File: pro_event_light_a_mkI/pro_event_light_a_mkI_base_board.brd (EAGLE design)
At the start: 39.4 x 59.4 mm, 32 parts, among them IC1 LT1936, IC2 LT1936

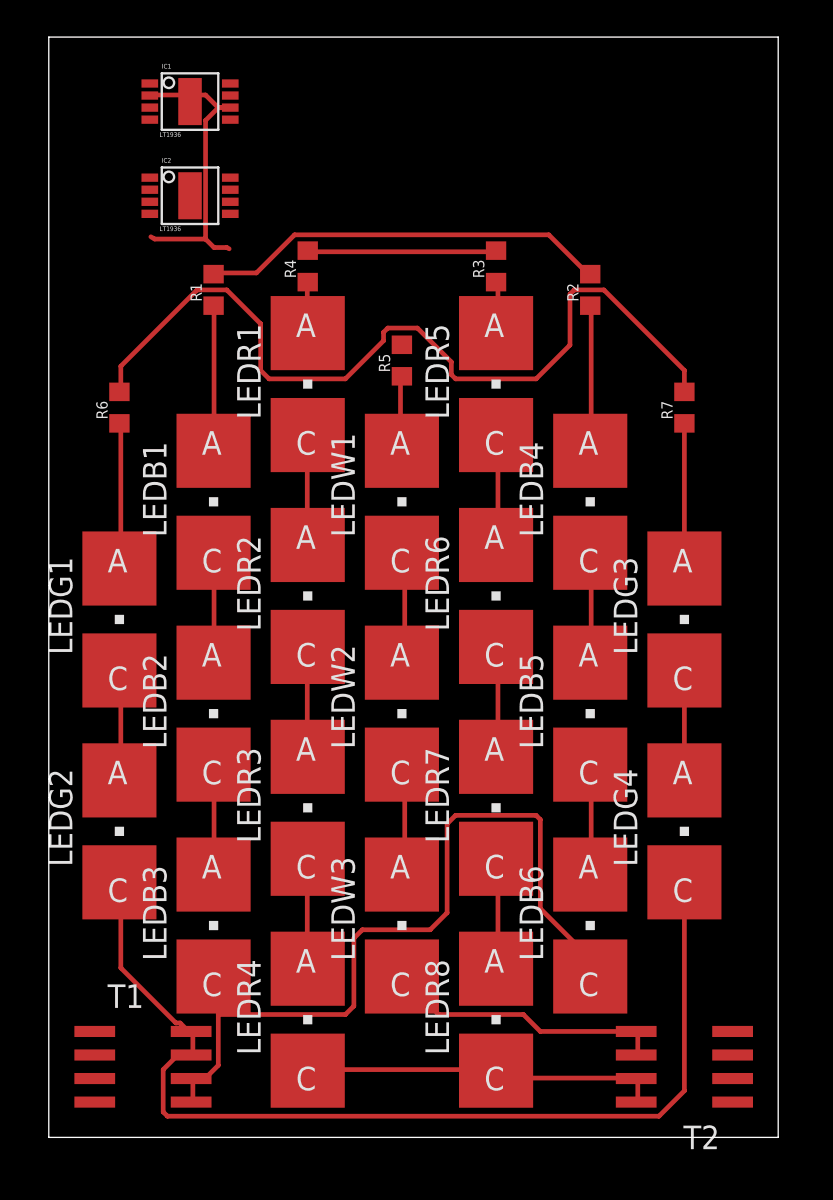
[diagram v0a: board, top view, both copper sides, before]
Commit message: now having the STM32L452 aboard as well as the LED controller from Infineon
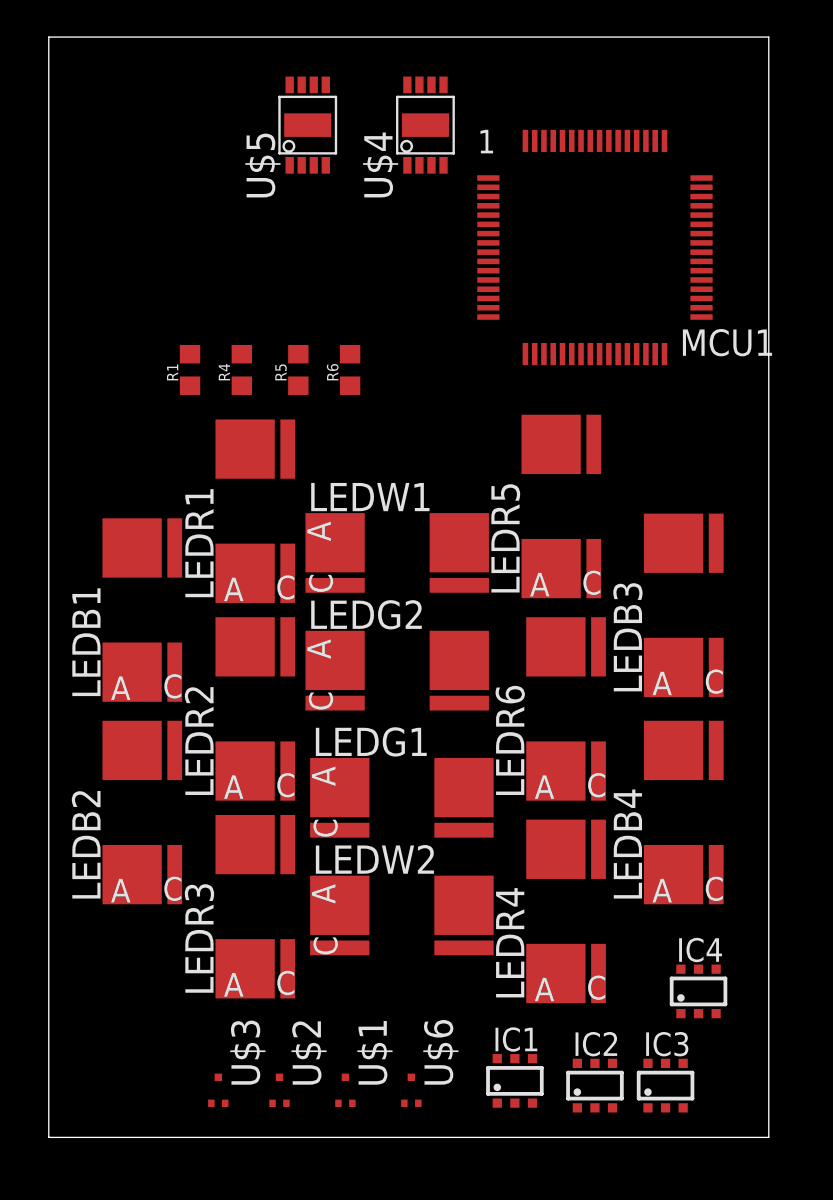
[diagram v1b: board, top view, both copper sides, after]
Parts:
- removed LEDB5, LEDB6, LEDG3, LEDG4, LEDR7, LEDR8, LEDW3: (no value), led:P-LCC-2
- removed R2, R3, R7: (no value), rcl:R0603
- removed T1, T2: (no value), zetex:SO8
- added IC3, IC4: ILD4001, infineon:SC74_INFINEON
- added MCU1: STM32L452RET6, mod_eagle_library_MCU_CPU:LQFP64
- added U$1, U$2, U$3, U$6: PMXB56EN, mod_eagle_library_discrete_elements:DFN1010D-3
- added U$4, U$5: LT1936, mod_eagle_library_pmic:MSOP8
- IC1, IC2: value LT1936 -> ILD4001; device mod_eagle_library_LINEAR_TECHNOLOGY:MSOP8 -> infineon:SC74_INFINEON
- LEDB1, LEDB2, LEDB3, LEDB4: value (none) -> LDG5AP; device led:P-LCC-2 -> mod_eagle_library_discrete_elements:P-LCC-2
- LEDG1, LEDG2: value (none) -> LTG5AP; device led:P-LCC-2 -> mod_eagle_library_discrete_elements:P-LCC-2
- LEDR1, LEDR2, LEDR3, LEDR4, LEDR5, LEDR6: value (none) -> LRG5AP; device led:P-LCC-2 -> mod_eagle_library_discrete_elements:P-LCC-2
- LEDW1, LEDW2: value (none) -> LCWG5GP; device led:P-LCC-2 -> mod_eagle_library_discrete_elements:P-LCC-2
- moved IC1 55.7 mm to (25.1, 3.05), turned to 0 degrees
- moved IC2 52.7 mm to (29.5, 2.79), turned to 0 degrees
- moved LEDB3 31.6 mm to (35.3, 28.7), turned to 90 degrees
- moved LEDG1 18.6 mm to (19.1, 17.3)
- moved LEDB4 17.8 mm to (35.3, 17.5), turned to 90 degrees
- moved LEDG2 16.8 mm to (18.8, 24.1)
- moved LEDR4 16.1 mm to (29.0, 12.2), turned to 90 degrees
- moved R6 12.6 mm to (16.3, 41.4)
- moved LEDW2 11.9 mm to (19.1, 10.9)
- moved LEDR5 8.03 mm to (28.7, 34.0), turned to 90 degrees
- moved LEDR6 7.78 mm to (29.0, 23.1), turned to 90 degrees
- moved LEDR1 7.08 mm to (12.2, 33.8), turned to 90 degrees
- moved R4 6.62 mm to (10.4, 41.4)
- moved LEDB1 6.48 mm to (6.10, 28.4), turned to 90 degrees
- moved LEDR2 6.35 mm to (12.2, 23.1), turned to 90 degrees
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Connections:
- removed net N$15: LEDG1.C, LEDG2.A
- removed net N$17: LEDR1.C, LEDR2.A
- removed net N$18: LEDW1.C, LEDW2.A
- removed net N$19: LEDR5.C, LEDR6.A
- removed net N$20: LEDB4.C, LEDB5.A
- removed net N$21: LEDG3.C, LEDG4.A
- removed net N$26: LEDR2.C, LEDR3.A
- removed net N$27: LEDB2.C, LEDB3.A
- removed net N$28: LEDR3.C, LEDR4.A
- removed net N$33: LEDR4.C, LEDR8.C, T2.7, T2.8
- removed net N$34: LEDW3.C, T2.5, T2.6
- new net GND: IC1.2, IC1.5, IC2.2, IC2.5, IC3.2, IC3.5, IC4.2, IC4.5
- new net N$12: LEDR3.3, LEDR3.4, LEDR4.1, LEDR4.2
- new net N$14: LEDR5.3, LEDR5.4, LEDR6.1, LEDR6.2
- net N$1: now also U$1.2, U$2.2, U$3.2; no longer LEDG1.A, R6.1
- net N$11: no longer R7.2
- net N$13: no longer R3.2
- net N$16: now also LEDR1.1, LEDR1.2, LEDR3.1, LEDR3.2, LEDR5.1, LEDR5.2, R4.1; no longer LEDB1.C, LEDB2.A
- net N$2: now also LEDG2.1, LEDG2.2, R6.1; no longer LEDB1.A, R1.1
- net N$22: now also LEDR2.3, LEDR2.4, LEDR4.3, LEDR4.4, LEDR6.3, LEDR6.4, U$2.3; no longer LEDB5.C, LEDB6.A
- net N$23: now also LEDW1.1, LEDW1.2, R5.1; no longer LEDR7.C, LEDR8.A
- net N$24: now also LEDW2.3, LEDW2.4, U$6.3; no longer LEDR6.C, LEDR7.A
- net N$25: now also LEDW1.3, LEDW1.4, LEDW2.1, LEDW2.2; no longer LEDW2.C, LEDW3.A
- net N$29: now also LEDG1.3, LEDG1.4, U$1.3; no longer LEDG2.C, LEDG4.C, T1.7, T1.8
- net N$3: now also LEDG1.1, LEDG1.2, LEDG2.3, LEDG2.4; no longer LEDR1.A, R4.1
- net N$31: now also LEDB2.3, LEDB2.4, LEDB4.3, LEDB4.4, U$3.3; no longer LEDB3.C, LEDB6.C, T1.5, T1.6
- net N$4: now also LEDB1.3, LEDB1.4, LEDB2.1, LEDB2.2; no longer LEDW1.A, R5.1
- net N$5: now also LEDB1.1, LEDB1.2, LEDB3.1, LEDB3.2, R1.1; no longer LEDR5.A, R3.1
- net N$6: now also LEDB3.3, LEDB3.4, LEDB4.1, LEDB4.2; no longer LEDB4.A, R2.1
- net N$7: now also LEDR1.3, LEDR1.4, LEDR2.1, LEDR2.2; no longer LEDG3.A, R7.1
- net N$8: no longer R2.2
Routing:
- net N$29: track 55.4 -> 0.00 mm
- net N$11: track 46.5 -> 0.00 mm
- net N$31: track 44.5 -> 0.00 mm
- net N$8: track 22.1 -> 0.00 mm
- net N$33: track 19.2 -> 0.00 mm
- net GND: track 16.9 -> 0.00 mm
- net N$34: track 15.3 -> 0.00 mm
- net N$13: track 10.2 -> 0.00 mm
- net N$1: track 7.87 -> 0.00 mm
- net N$6: track 7.85 -> 0.00 mm
- net N$2: track 7.84 -> 0.00 mm
- net N$7: track 7.83 -> 0.00 mm
- net N$19: track 6.02 -> 0.00 mm
- net N$24: track 6.02 -> 0.00 mm
- net N$23: track 6.02 -> 0.00 mm
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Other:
- board size 39.4 x 59.4 mm -> 38.8 x 59.4 mm

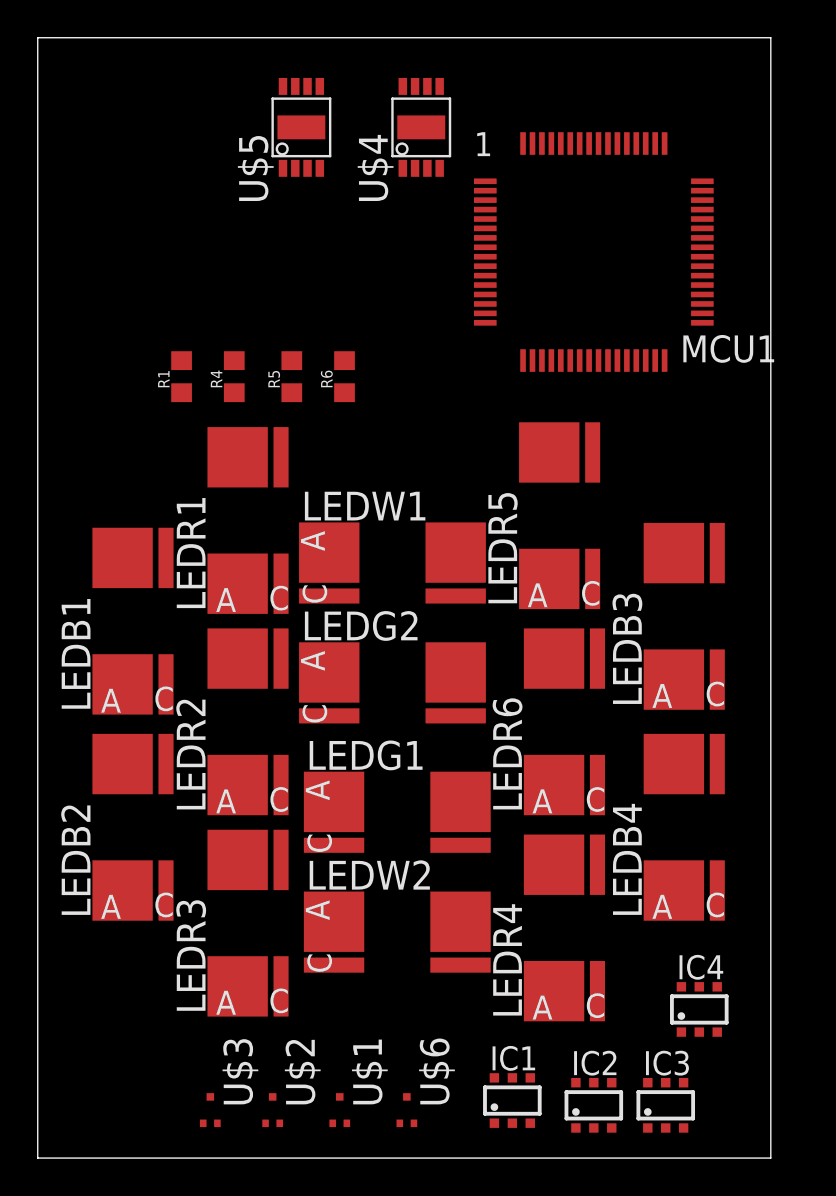
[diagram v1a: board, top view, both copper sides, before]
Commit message: included rotary switch (also in separate library)
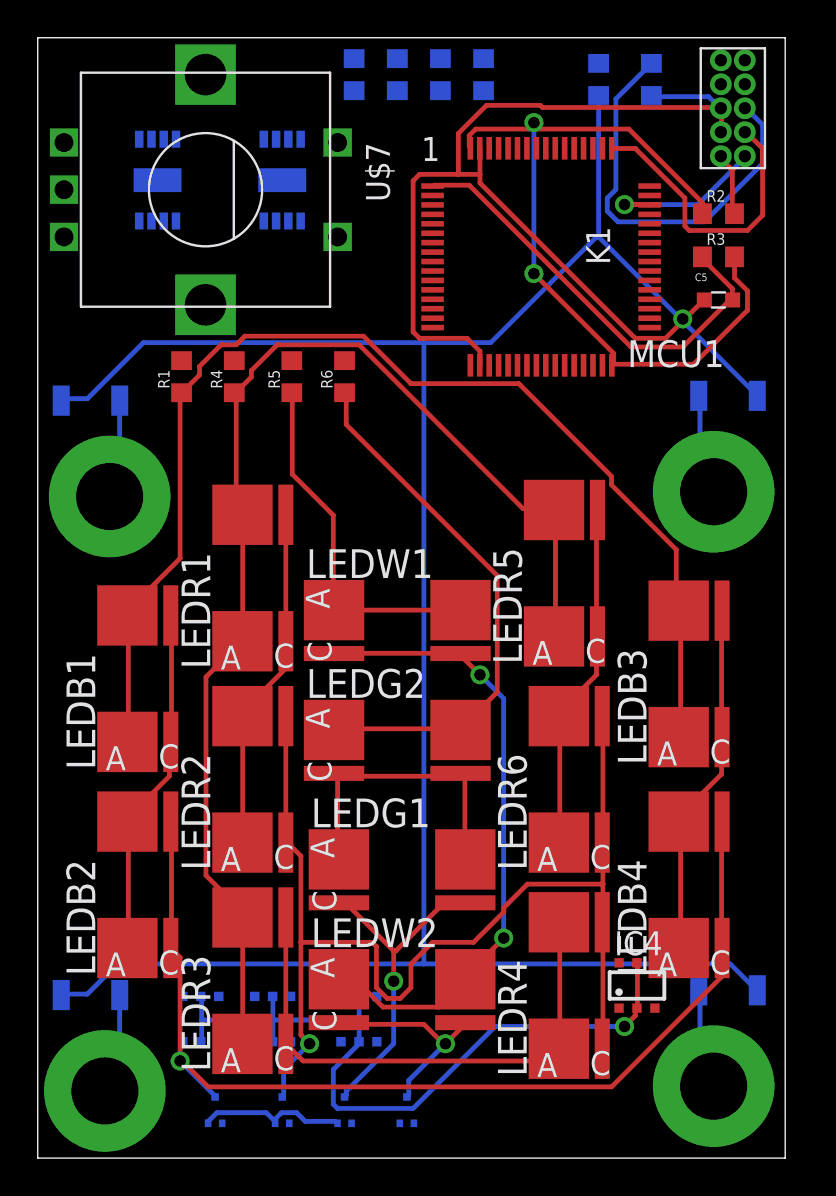
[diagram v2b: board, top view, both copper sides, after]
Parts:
- added C1, C29, C34, C35: 1uF, Eagle_Wurth_Elektronik_Passive_Capacitors_rev15a:WCAP-CSGP_1206
- added C5: 100nF, Eagle_Wurth_Elektronik_Passive_Capacitors_rev15a:WCAP-CSGP_0603_REFLOW
- added K1: 62201021121, Board_to_Board_Connectors_rev15d:62201021121
- added R10, R3, R7, R8, R9: 0R0, rcl:R0603
- added R2: (no value), rcl:R0603
- added R35, R36: 0R, rcl:R0603
- added U$10, U$11, U$15, U$8: (no value), mod-eagle_library_standard_passive_parts:PCB_MOUNTING_HOLES_M3
- added U$7: ALPS_EC11D, mod_eagle_library_switches:ALPS_EC11D
- moved IC2 17.6 mm to (12.4, 7.37), flipped to the bottom
- moved IC1 17.1 mm to (8.64, 7.37), flipped to the bottom
- moved IC3 16.9 mm to (17.0, 7.37), flipped to the bottom
- moved U$5 8.12 mm to (6.35, 51.8), flipped to the bottom, turned to 180 degrees
- moved U$4 7.88 mm to (13.0, 51.8), flipped to the bottom, turned to 180 degrees
- moved IC4 3.54 mm to (31.8, 9.14)
- moved LEDB3 3.06 mm to (35.6, 25.7)
- moved LEDB1 3.06 mm to (6.35, 25.4)
- moved LEDR2 3.06 mm to (12.4, 20.1)
- moved LEDR5 3.06 mm to (29.0, 31.0)
- moved LEDR6 3.06 mm to (29.2, 20.1)
- moved LEDW1 3.06 mm to (19.1, 27.4)
- moved LEDB4 3.06 mm to (35.6, 14.5)
- moved LEDW2 3.06 mm to (19.3, 7.87)
- moved LEDB2 3.06 mm to (6.35, 14.5)
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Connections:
- new net GND_MCU: C1.2, C29.2, C34.2, C35.2, C5.1, K1.2, K1.3, MCU1.18, MCU1.47, MCU1.63, R10.2, R35.2, R36.2, R7.2, R8.2, R9.2
- new net N$15: C34.1, U$10.PIN1
- new net N$17: C35.1, U$15.PIN1
- new net N$18: C1.1, U$8.PIN1
- new net N$19: C5.2, MCU1.1, R3.1
- new net N$20: MCU1.3, R10.1
- new net N$21: R8.1
- new net N$26: MCU1.5, R9.1
- new net N$27: MCU1.6, R7.1
- new net N$9: C29.1, U$11.PIN1
- new net NRESET: K1.6
- new net S3V3_MCU_VDD: MCU1.19, MCU1.32, MCU1.64, R2.1, R3.2
- new net SWCLK: K1.9, MCU1.49
- new net SWDIO: K1.10, MCU1.46
- new net SWO: K1.8, R35.1
- new net TDI: K1.7, R36.1
- new net VTREF: K1.1, R2.2
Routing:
- net GND_MCU: track 0.00 -> 179.1 mm, vias 0 -> 1
- net N$16: track 0.00 -> 65.0 mm
- net N$5: track 0.00 -> 62.5 mm
- net N$22: track 0.00 -> 60.9 mm, vias 0 -> 1
- net N$31: track 0.00 -> 55.5 mm, vias 0 -> 1
- net S3V3_MCU_VDD: track 0.00 -> 41.9 mm, vias 0 -> 2
- net GND: track 0.00 -> 40.5 mm, vias 0 -> 1
- net N$25: track 0.00 -> 33.7 mm, vias 0 -> 2
- net N$2: track 0.00 -> 28.8 mm
- net N$12: track 0.00 -> 28.6 mm
- net N$19: track 0.00 -> 23.5 mm
- net SWO: track 0.00 -> 21.9 mm
- net N$23: track 0.00 -> 19.2 mm
- net N$6: track 0.00 -> 18.9 mm
- net N$4: track 0.00 -> 18.6 mm
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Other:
- board size 38.8 x 59.4 mm -> 39.6 x 59.4 mm

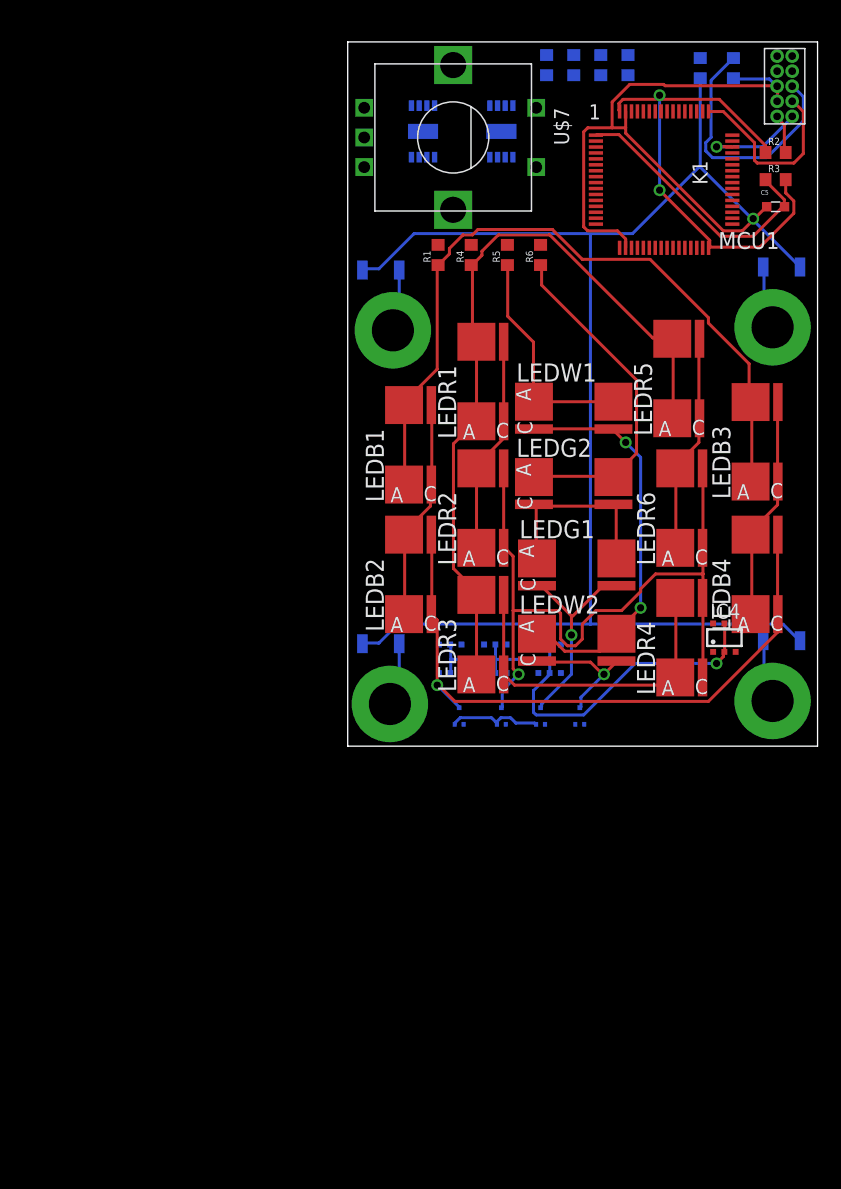
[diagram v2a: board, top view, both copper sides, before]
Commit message: some comments and periphery on LT1936
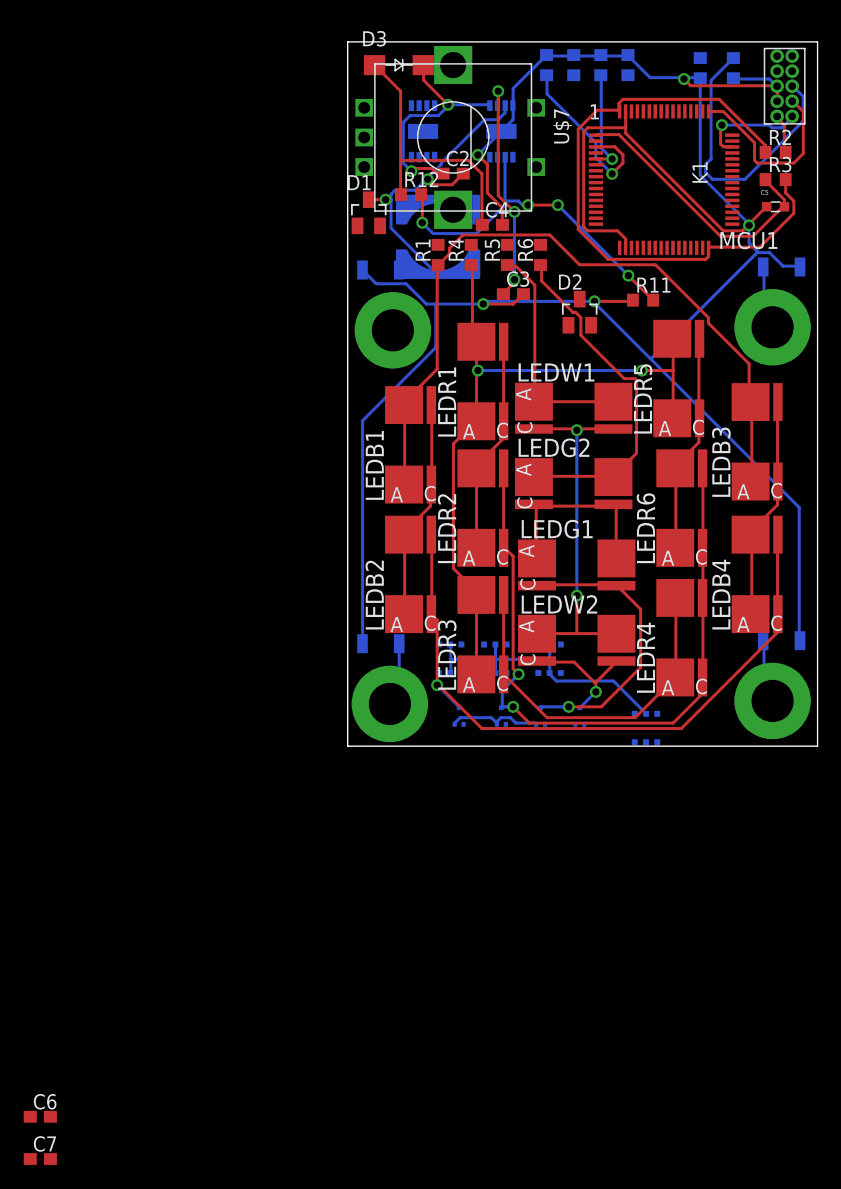
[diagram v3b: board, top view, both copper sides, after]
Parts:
- added C2, C3, C4, C6, C7: (no value), rcl:C0603
- added D1, D2: BAS40, diode:SOT23
- added D3: GF1, diode:SMA-DO214AC
- added L1: MSS7341, inductor-coilcraft:MSS7341
- added R11, R12: (no value), rcl:R0603
- moved IC4 10.1 mm to (25.1, 1.52), flipped to the bottom
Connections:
- new net N$28: U$4.7
- new net N$30: C3.1, C6.1, U$4.2
- new net N$33: C2.1, D3.K, U$4.1
- new net N$34: C2.2, D1.3, L1.2, U$4.3
- new net N$35: R11.2, R12.2, U$4.6
- new net N$36: C4.1, C7.1, D3.A, L1.1, R12.1
- net GND_MCU: now also C3.2, C4.2, C6.2, C7.2, D1.1, R11.1, U$4.4, U$4.9
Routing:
- net N$35: track 0.00 -> 30.7 mm, vias 0 -> 4
- net GND_MCU: track 179.1 -> 207.9 mm, vias 1 -> 5
- net N$34: track 0.00 -> 27.1 mm, vias 0 -> 2
- net N$36: track 0.00 -> 23.5 mm
- net N$33: track 0.00 -> 19.6 mm, vias 0 -> 2
- net N$30: track 0.00 -> 19.3 mm, vias 0 -> 3
- net GND: track 40.5 -> 25.2 mm, vias 1 -> 0
- net N$20: track 0.00 -> 15.1 mm, vias 0 -> 1
- net S3V3_MCU_VDD: track 41.9 -> 52.3 mm, vias 2 -> 0
- net N$26: track 0.00 -> 8.82 mm, vias 0 -> 1
- net N$29: track 17.6 -> 24.4 mm
- net N$17: track 5.32 -> 0.00 mm
- net N$16: track 65.0 -> 59.7 mm, vias 0 -> 2
- net N$25: track 33.7 -> 30.7 mm
- net SWO: track 21.9 -> 24.5 mm
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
